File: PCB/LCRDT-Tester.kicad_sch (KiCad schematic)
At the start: 11 parts, among them SW1 SW_Push

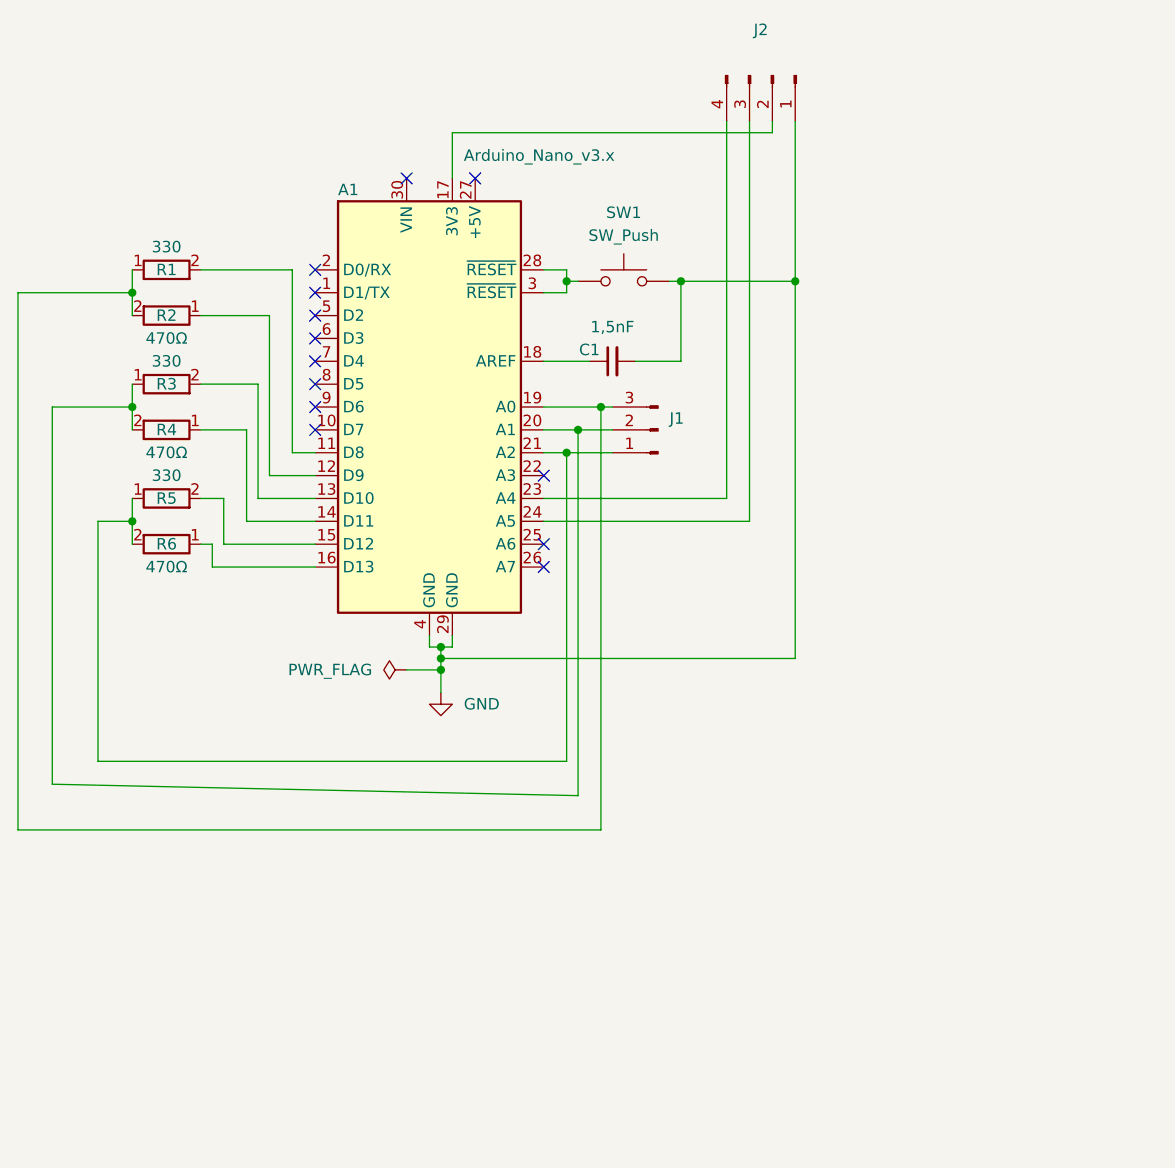
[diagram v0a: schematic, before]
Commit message: -added m3 mounting hole -added start button -more compact design -added logos -added 3d arduino shapes wrl -updated docs & readme -updated code
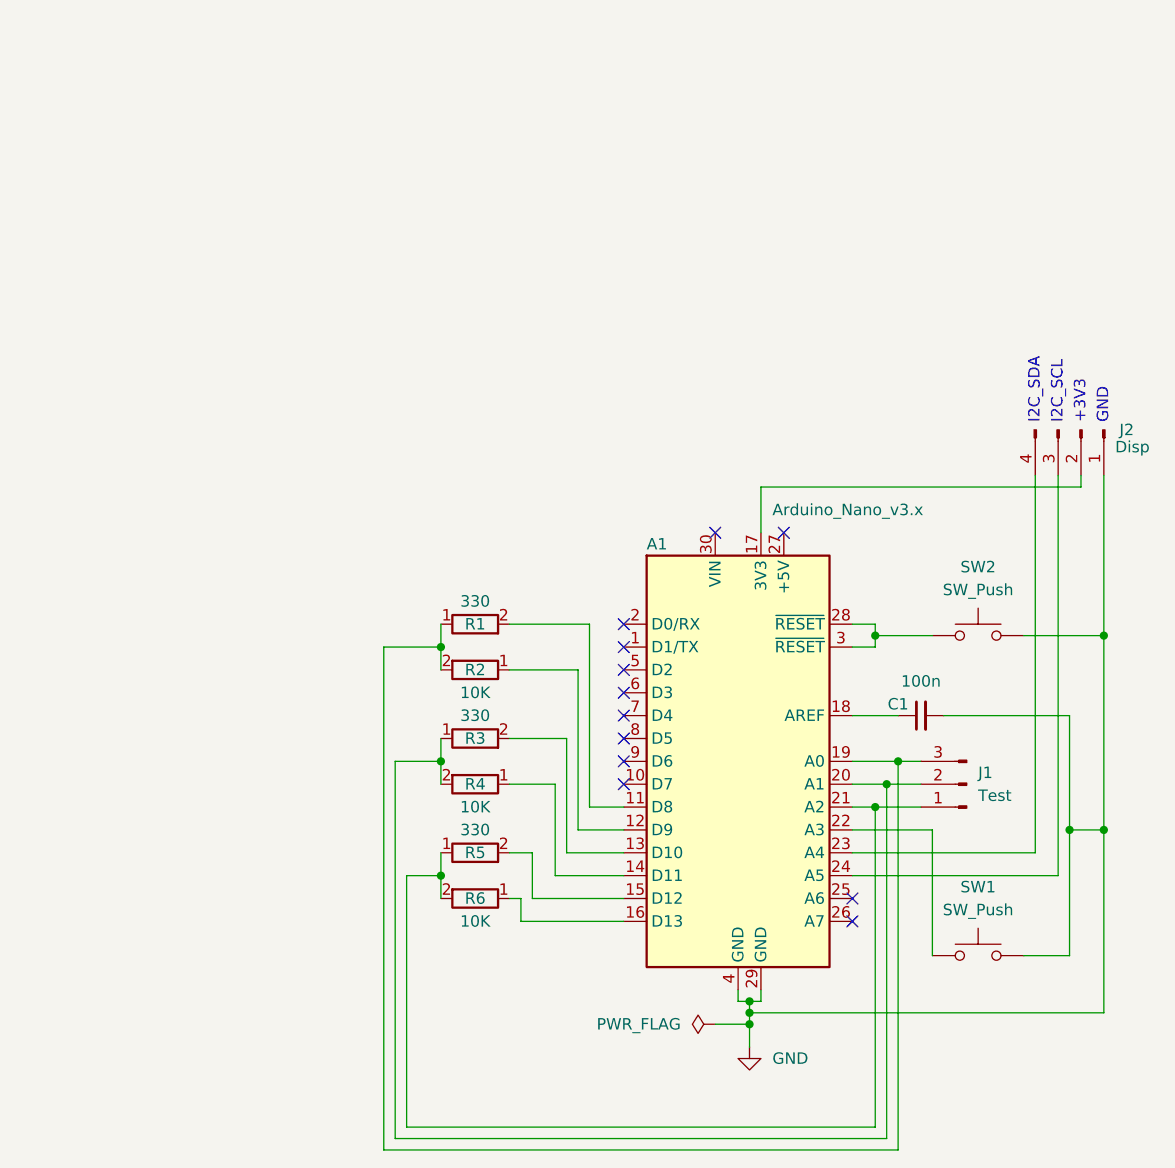
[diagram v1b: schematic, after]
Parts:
- added SW2: SW_Push, Button_Switch_THT:SW_PUSH_1P1T_6x3.5mm_H4.3_APEM_MJTP1243, symbol Switch:SW_Push
- C1: value 1,5nF -> 100n
- J1: value (none) -> Test
- J2: value (none) -> Disp
- R2, R4, R6: value 470Ω -> 10K
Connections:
- net GND: now also SW2.2
- net at A1.28 (~{RESET}), A1.3 (~{RESET}): now also SW2.1; no longer SW1.1
- net at A1.22 (A3): now also SW1.1
- no-connect marks 13 -> 12
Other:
- note added: "+3V3"
- note added: "GND"
- note added: "I2C_SCL"
- note added: "I2C_SDA"
- title: LCRD-Tester -> LCRDT-Tester
- moved on the sheet: A1, C1, J1, J2, R1, R2, R3, R4, R5, R6

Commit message: cleanups+Mountingholes
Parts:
- A1: footprint Module:Arduino_Nano -> Module:Arduino_Nano_WithMountingHoles
